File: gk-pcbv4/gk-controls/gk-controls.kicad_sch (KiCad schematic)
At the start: 36 parts, among them J1 Conn_01x20, U1 PCAL6416APW, U2 ULN2003A

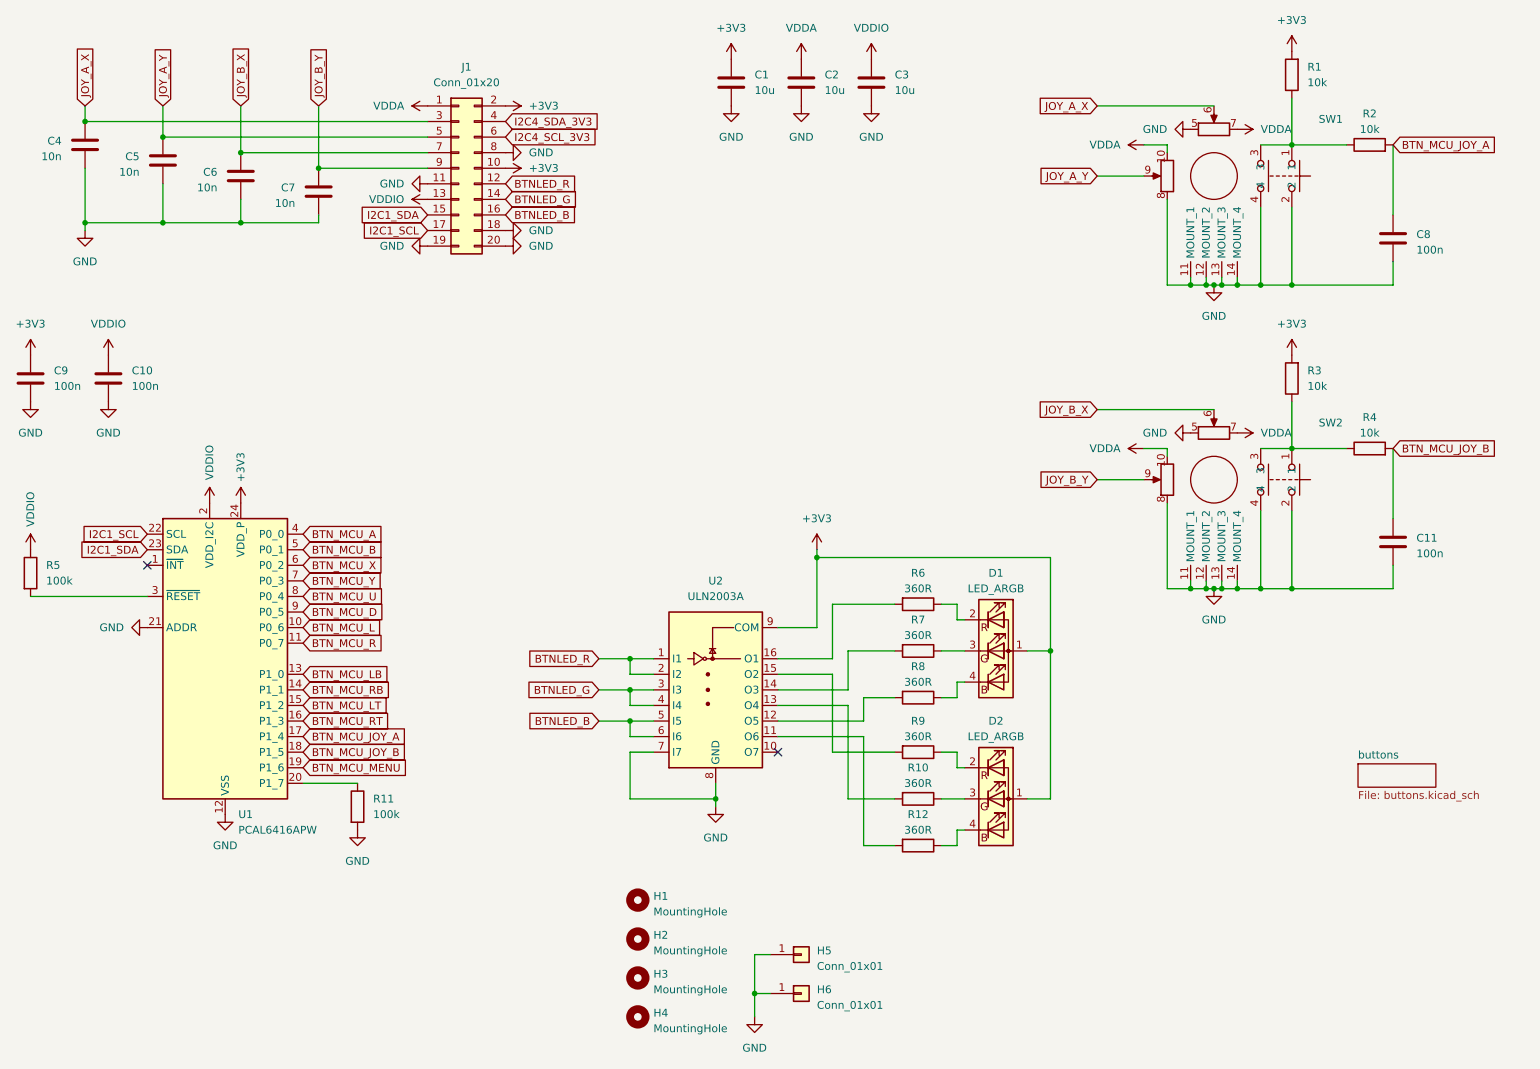
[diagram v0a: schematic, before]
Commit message: add v2 controls board
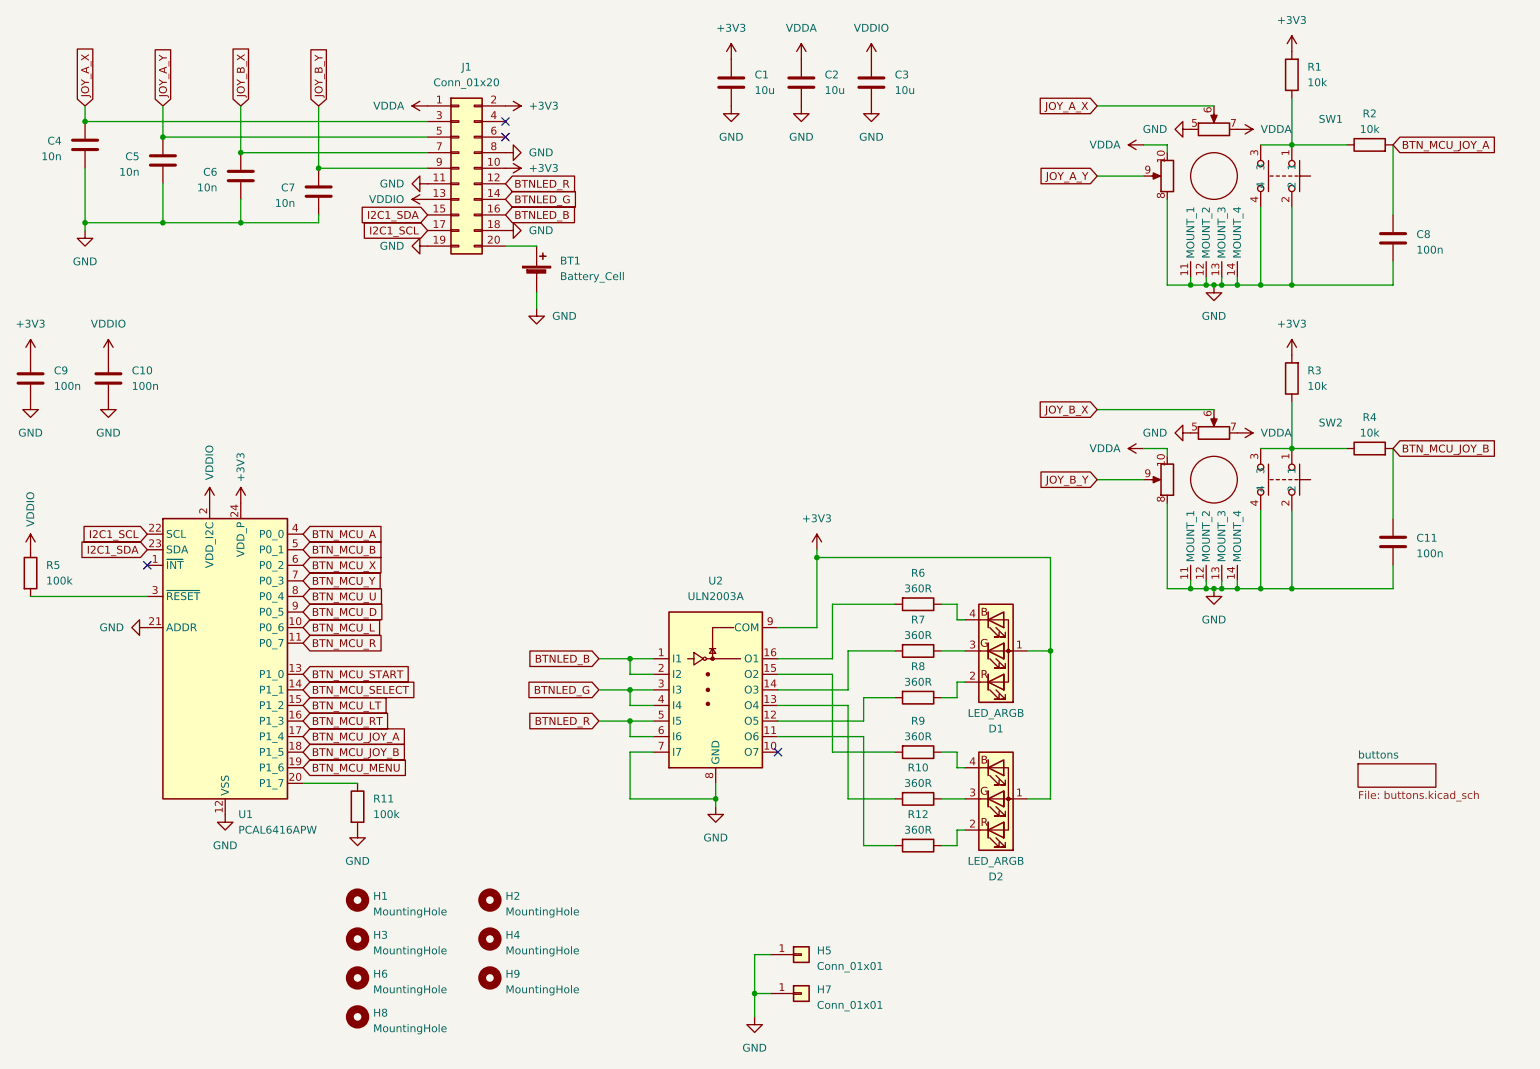
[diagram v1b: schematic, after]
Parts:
- added BT1: Battery_Cell, Battery:BatteryHolder_Keystone_3002_1x2032, symbol Device:Battery_Cell
- added H2, H4, H9: MountingHole, MountingHole:MountingHole_3.2mm_M3, symbol Mechanical:MountingHole
- renumbered H2 to H3, H3 to H6, H6 to H7, H4 to H8
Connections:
- net BTNLED_B: now also U2.1 (I1), U2.2 (I2); no longer U2.5 (I5), U2.6 (I6)
- net BTNLED_R: now also U2.5 (I5), U2.6 (I6); no longer U2.1 (I1), U2.2 (I2)
- net GND: now also BT1.2 (-); no longer J1.20 (Pin_20)
- net at R8.1: now also D1.2 (RK); no longer D1.4 (BK)
- net at D2.2 (RK): now also R12.1; no longer R9.1
- net at D2.4 (BK): now also R9.1; no longer R12.1
- net at R6.1: now also D1.4 (BK); no longer D1.2 (RK)
- net BTN_MCU_LB renamed BTN_MCU_START
- net BTN_MCU_RB renamed BTN_MCU_SELECT
- net I2C4_SCL_3V3: no longer names the net of J1.6 (Pin_6)
- net I2C4_SDA_3V3: no longer names the net of J1.4 (Pin_4)
- new net: BT1.1 (+), J1.20 (Pin_20)
- no-connect marks 2 -> 4
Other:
- moved on the sheet: D1, D2, H1, H3, H6, H8

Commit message: merge control board after trigger added
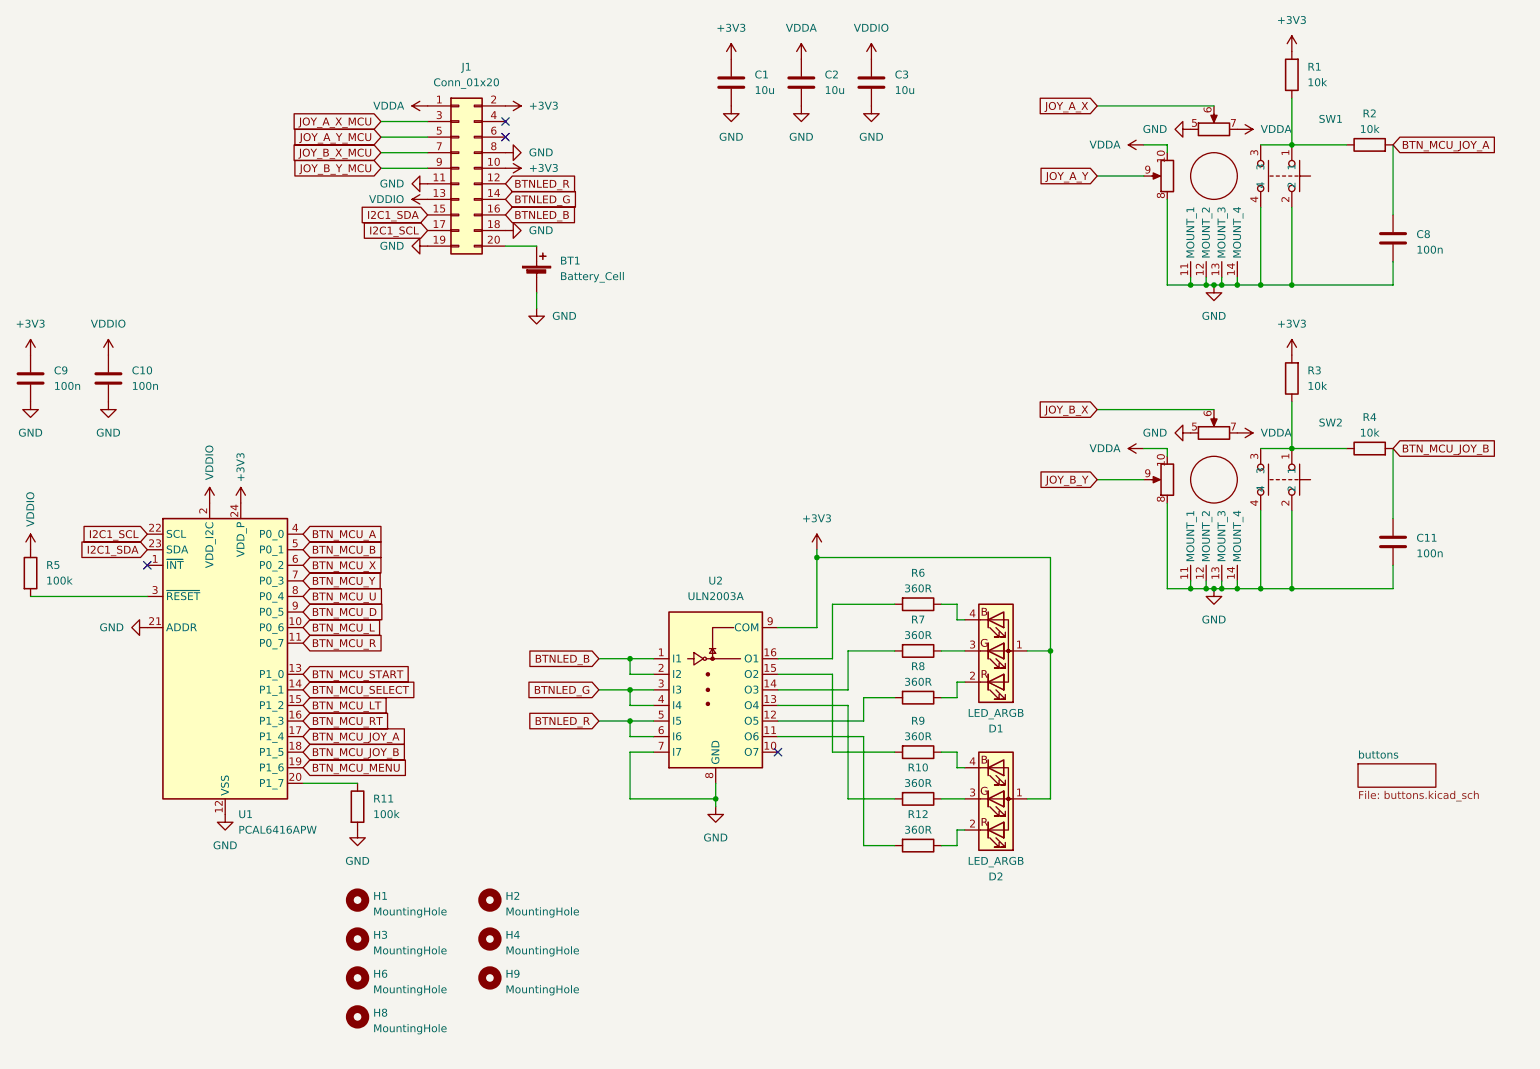
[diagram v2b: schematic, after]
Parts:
- removed C4, C5, C6, C7: 10n, Capacitor_SMD:C_0603_1608Metric, symbol Device:C
- removed H5, H7: Conn_01x01, Connector_PinHeader_2.54mm:PinHeader_1x01_P2.54mm_Vertical, symbol Connector_Generic:Conn_01x01
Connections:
- net JOY_A_X: no longer J1.3 (Pin_3)
- net JOY_A_Y: no longer J1.5 (Pin_5)
- net JOY_B_X: no longer J1.7 (Pin_7)
- net JOY_B_Y: no longer J1.9 (Pin_9)
- new net JOY_A_X_MCU: J1.3 (Pin_3)
- new net JOY_A_Y_MCU: J1.5 (Pin_5)
- new net JOY_B_X_MCU: J1.7 (Pin_7)
- new net JOY_B_Y_MCU: J1.9 (Pin_9)
